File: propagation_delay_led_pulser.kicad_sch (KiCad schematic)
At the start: 16 parts, among them J1 Power/Bias In, J4 Pulse Out, U1 ICM7555xB, U2 74AC14, U3 74AHC1G00

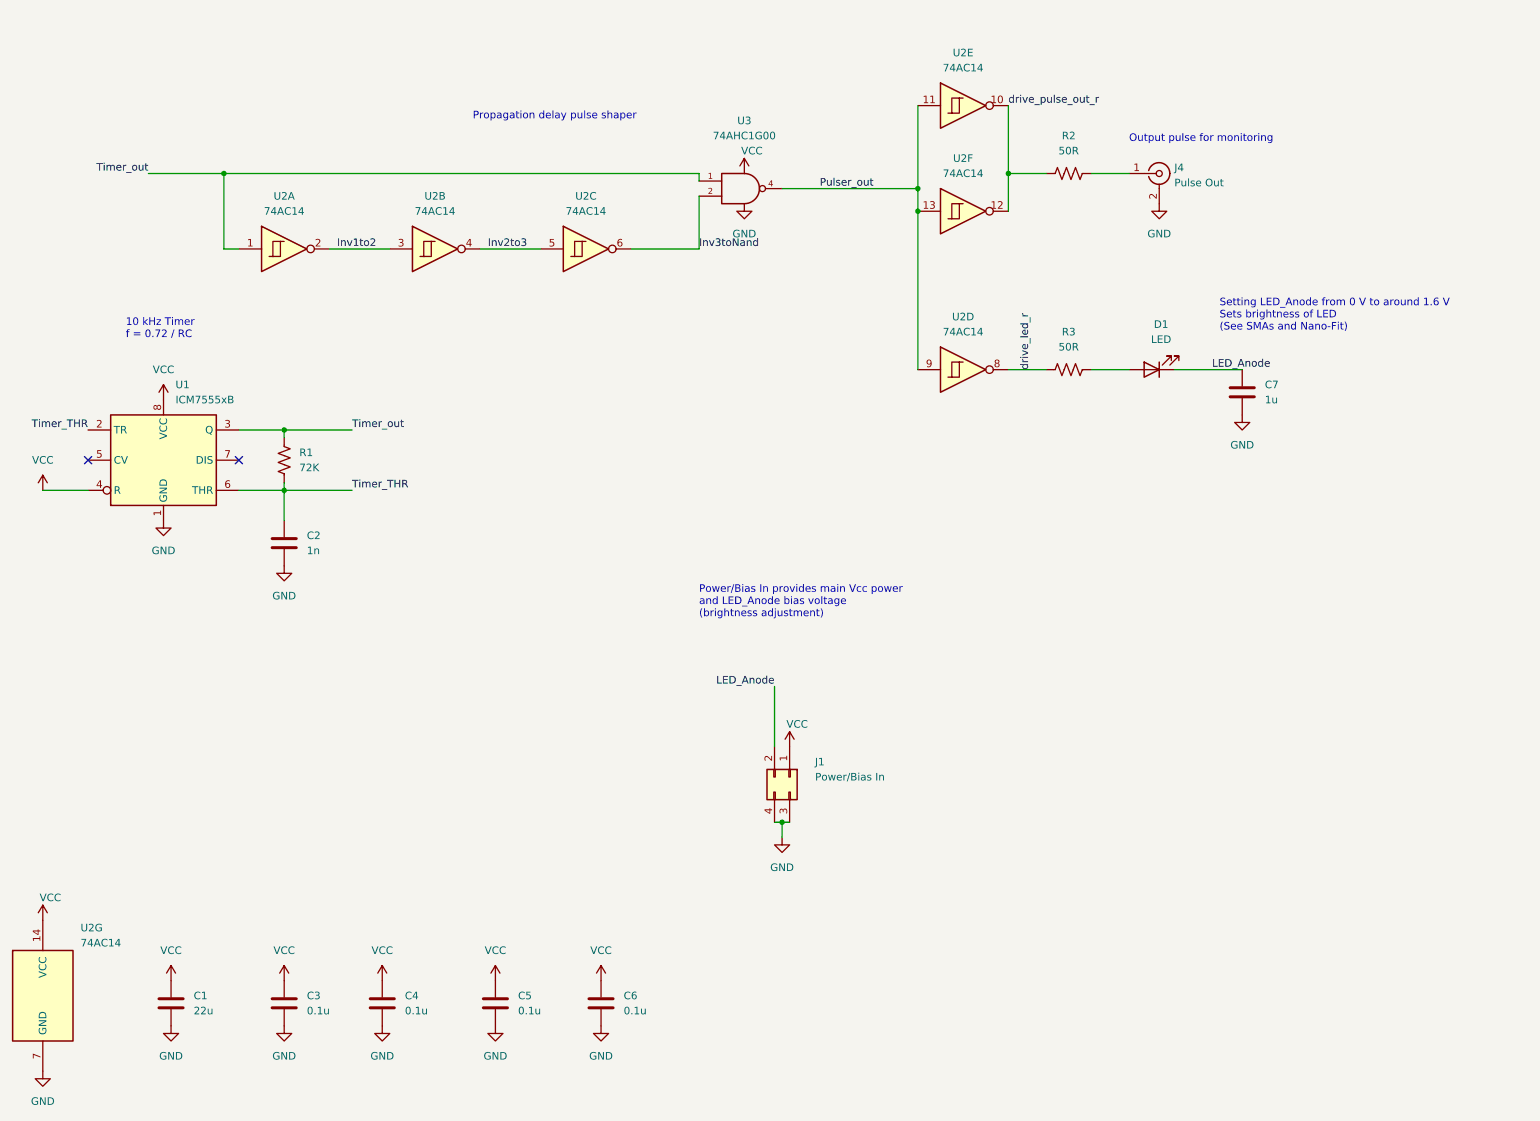
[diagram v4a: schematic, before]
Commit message: most routing done, need to poar ground plane
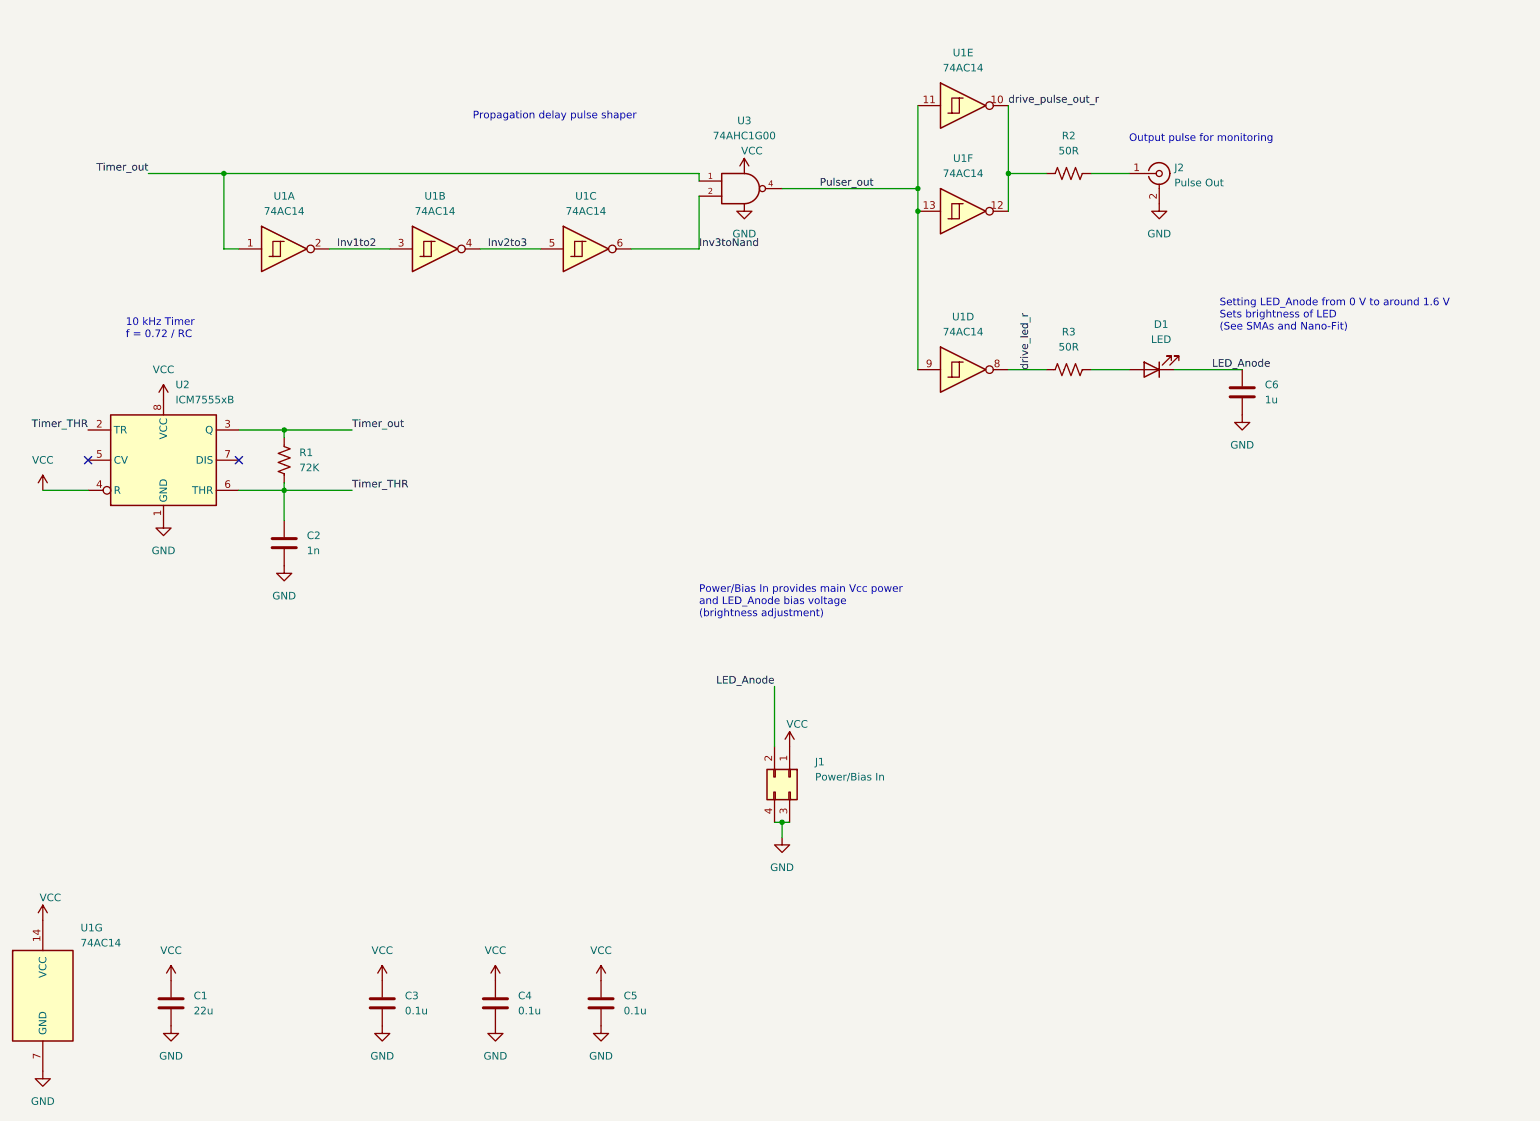
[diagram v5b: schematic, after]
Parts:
- removed C3: 0.1u, Resistor_SMD:R_0612_1632Metric_Pad1.18x3.40mm_HandSolder, symbol Device:C
- U1: renamed from U2; footprint (none) -> Package_SO:SOIC-14_3.9x8.7mm_P1.27mm
- renumbered C4 to C3, C5 to C4, C6 to C5, C7 to C6, J4 to J2, U1 to U2

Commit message: PCB layout complete
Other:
- company: Hugon Labs -> HugonLabs
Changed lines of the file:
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@@
   (title_block
     (title "Propagation Delay LED Pulser")
-    (date "2022-02-21")
-    (rev "v0.1")
-    (company "Hugon Labs")
+    (date "2022-02-28")
+    (rev "1.0")
+    (company "HugonLabs")
   )
   (junction (at 170.18 46.99) (diameter 0) (color 0 0 0 0)

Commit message: Removed extra vias and changed 0612 caps to 1206
  should ease soldering greatly
  Hopefully all done for v1.1
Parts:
- C1: footprint Resistor_SMD:R_1206_3216Metric_Pad1.30x1.75mm_HandSolder -> Capacitor_SMD:C_1206_3216Metric_Pad1.33x1.80mm_HandSolder
- C3, C4, C5: footprint Resistor_SMD:R_0612_1632Metric_Pad1.18x3.40mm_HandSolder -> Capacitor_SMD:C_1206_3216Metric_Pad1.33x1.80mm_HandSolder; Mfr Kyocera AVX -> Samsung; Part 06125C104KAT2A -> CL31B104KBCNNND
- C6: footprint Resistor_SMD:R_0612_1632Metric_Pad1.18x3.40mm_HandSolder -> Capacitor_SMD:C_1206_3216Metric_Pad1.33x1.80mm_HandSolder; Mfr Kyocera AVX -> Samsung; Part 0612YC105KAT2A -> CL31B105KBHNFNE
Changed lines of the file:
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@@
   (title_block
     (title "Propagation Delay LED Pulser")
-    (date "2022-02-28")
-    (rev "1.0")
+    (date "2022-04-12")
+    (rev "1.1")
     (company "HugonLabs")
   )
@@
       (effects (font (size 1.27 1.27)) hide)
     )
+    (pin "1")
+    (pin "2")
+    (pin "3")
+    (pin "4")
+    (pin "5")
+    (pin "6")
+    (pin "8")
+    (pin "9")
+    (pin "10")
+    (pin "11")
     (pin "12")
     (pin "13")
+    (pin "14")
+    (pin "7")
   )
   (symbol (lib_id "power:GND") (at 140.97 45.72 0) (unit 1)
@@
       (effects (font (size 1.27 1.27)) (justify left))
     )
-    (property "Footprint" "Resistor_SMD:R_0612_1632Metric_Pad1.18x3.40mm_HandSolder" (id 2) (at 225.7552 81.28 0)
-      (effects (font (size 1.27 1.27)) hide)
-    )
-    (property "Datasheet" "https://www.mouser.com/datasheet/2/40/AVXCS06407_1-2538087.pdf" (id 3) (at 224.79 77.47 0)
-      (effects (font (size 1.27 1.27)) hide)
-    )
-    (property "Mfr" "Kyocera AVX" (id 4) (at 224.79 77.47 0)
-      (effects (font (size 1.27 1.27)) hide)
-    )
-    (property "Part" "0612YC105KAT2A" (id 5) (at 224.79 77.47 0)
+    (property "Footprint" "Capacitor_SMD:C_1206_3216Metric_Pad1.33x1.80mm_HandSolder" (id 2) (at 225.7552 81.28 0)
+      (effects (font (size 1.27 1.27)) hide)
+    )
+    (property "Datasheet" "https://www.mouser.com/datasheet/2/585/MLCC-1837944.pdf" (id 3) (at 224.79 77.47 0)
+      (effects (font (size 1.27 1.27)) hide)
+    )
+    (property "Mfr" "Samsung" (id 4) (at 224.79 77.47 0)
+      (effects (font (size 1.27 1.27)) hide)
+    )
+    (property "Part" "CL31B105KBHNFNE" (id 5) (at 224.79 77.47 0)
       (effects (font (size 1.27 1.27)) hide)
     )
@@
     (pin "1")
     (pin "2")
+    (pin "3")
+    (pin "4")
+    (pin "5")
+    (pin "6")
+    (pin "8")
+    (pin "9")
+    (pin "10")
+    (pin "11")
+    (pin "12")
+    (pin "13")
+    (pin "14")
+    (pin "7")
   )
   (symbol (lib_id "power:VCC") (at 22.86 166.37 0) (unit 1)
@@
       (effects (font (size 1.27 1.27)) hide)
     )
+    (pin "1")
+    (pin "2")
+    (pin "3")
+    (pin "4")
+    (pin "5")
+    (pin "6")
     (pin "8")
     (pin "9")
+    (pin "10")
+    (pin "11")
+    (pin "12")
+    (pin "13")
+    (pin "14")
+    (pin "7")
   )
   (symbol (lib_id "74xx:74HC14") (at 114.3 53.34 0) (unit 3)
@@
       (effects (font (size 1.27 1.27)) hide)
     )
+    (pin "1")
+    (pin "2")
+    (pin "3")
+    (pin "4")
     (pin "5")
     (pin "6")
+    (pin "8")
+    (pin "9")
+    (pin "10")
+    (pin "11")
+    (pin "12")
+    (pin "13")
+    (pin "14")
+    (pin "7")
   )
   (symbol (lib_id "power:VCC") (at 99.06 176.53 0) (unit 1)
@@
       (effects (font (size 1.27 1.27)) hide)
     )
+    (pin "1")
+    (pin "2")
     (pin "3")
     (pin "4")
+    (pin "5")
+    (pin "6")
+    (pin "8")
+    (pin "9")
+    (pin "10")
+    (pin "11")
+    (pin "12")
+    (pin "13")
+    (pin "14")
+    (pin "7")
   )
   (symbol (lib_id "power:GND") (at 99.06 184.15 0) (unit 1)
@@
       (effects (font (size 1.27 1.27)) (justify left))
     )
-    (property "Footprint" "Resistor_SMD:R_0612_1632Metric_Pad1.18x3.40mm_HandSolder" (id 2) (at 80.9752 184.15 0)
-      (effects (font (size 1.27 1.27)) hide)
-    )
-    (property "Datasheet" "https://www.mouser.com/datasheet/2/40/AVXCS06407_1-2538087.pdf" (id 3) (at 80.01 180.34 0)
-      (effects (font (size 1.27 1.27)) hide)
-    )
-    (property "Mfr" "Kyocera AVX" (id 4) (at 80.01 180.34 0)
-      (effects (font (size 1.27 1.27)) hide)
-    )
-    (property "Part" "06125C104KAT2A" (id 5) (at 80.01 180.34 0)
+    (property "Footprint" "Capacitor_SMD:C_1206_3216Metric_Pad1.33x1.80mm_HandSolder" (id 2) (at 80.9752 184.15 0)
+      (effects (font (size 1.27 1.27)) hide)
+    )
+    (property "Datasheet" "https://www.mouser.com/datasheet/2/585/MLCC-1837944.pdf" (id 3) (at 80.01 180.34 0)
+      (effects (font (size 1.27 1.27)) hide)
+    )
+    (property "Mfr" "Samsung" (id 4) (at 80.01 180.34 0)
+      (effects (font (size 1.27 1.27)) hide)
+    )
+    (property "Part" "CL31B104KBCNNND" (id 5) (at 80.01 180.34 0)
       (effects (font (size 1.27 1.27)) hide)
     )
@@
       (effects (font (size 1.27 1.27)) (justify left))
     )
-    (property "Footprint" "Resistor_SMD:R_1206_3216Metric_Pad1.30x1.75mm_HandSolder" (id 2) (at 45.4152 184.15 0)
+    (property "Footprint" "Capacitor_SMD:C_1206_3216Metric_Pad1.33x1.80mm_HandSolder" (id 2) (at 45.4152 184.15 0)
       (effects (font (size 1.27 1.27)) hide)
     )
@@
       (effects (font (size 1.27 1.27)) (justify left))
     )
-    (property "Footprint" "Resistor_SMD:R_0612_1632Metric_Pad1.18x3.40mm_HandSolder" (id 2) (at 100.0252 184.15 0)
-      (effects (font (size 1.27 1.27)) hide)
-    )
-    (property "Datasheet" "https://www.mouser.com/datasheet/2/40/AVXCS06407_1-2538087.pdf" (id 3) (at 99.06 180.34 0)
-      (effects (font (size 1.27 1.27)) hide)
-    )
-    (property "Mfr" "Kyocera AVX" (id 4) (at 99.06 180.34 0)
-      (effects (font (size 1.27 1.27)) hide)
-    )
-    (property "Part" "06125C104KAT2A" (id 5) (at 99.06 180.34 0)
+    (property "Footprint" "Capacitor_SMD:C_1206_3216Metric_Pad1.33x1.80mm_HandSolder" (id 2) (at 100.0252 184.15 0)
+      (effects (font (size 1.27 1.27)) hide)
+    )
+    (property "Datasheet" "https://www.mouser.com/datasheet/2/585/MLCC-1837944.pdf" (id 3) (at 99.06 180.34 0)
+      (effects (font (size 1.27 1.27)) hide)
+    )
+    (property "Mfr" "Samsung" (id 4) (at 99.06 180.34 0)
+      (effects (font (size 1.27 1.27)) hide)
+    )
+    (property "Part" "CL31B104KBCNNND" (id 5) (at 99.06 180.34 0)
       (effects (font (size 1.27 1.27)) hide)
     )
@@
       (effects (font (size 1.27 1.27)) hide)
     )
+    (pin "1")
+    (pin "2")
+    (pin "3")
+    (pin "4")
+    (pin "5")
+    (pin "6")
+    (pin "8")
+    (pin "9")
+    (pin "10")
+    (pin "11")
+    (pin "12")
+    (pin "13")
     (pin "14")
     (pin "7")
@@
       (effects (font (size 1.27 1.27)) hide)
     )
+    (pin "1")
+    (pin "2")
+    (pin "3")
+    (pin "4")
+    (pin "5")
+    (pin "6")
+    (pin "8")
+    (pin "9")
     (pin "10")
     (pin "11")
+    (pin "12")
+    (pin "13")
+    (pin "14")
+    (pin "7")
   )
   (symbol (lib_id "Device:C") (at 63.5 102.87 0) (unit 1)
@@
       (effects (font (size 1.27 1.27)) (justify left))
     )
-    (property "Footprint" "Resistor_SMD:R_0612_1632Metric_Pad1.18x3.40mm_HandSolder" (id 2) (at 117.8052 184.15 0)
-      (effects (font (size 1.27 1.27)) hide)
-    )
-    (property "Datasheet" "https://www.mouser.com/datasheet/2/40/AVXCS06407_1-2538087.pdf" (id 3) (at 116.84 180.34 0)
-      (effects (font (size 1.27 1.27)) hide)
-    )
-    (property "Mfr" "Kyocera AVX" (id 4) (at 116.84 180.34 0)
-      (effects (font (size 1.27 1.27)) hide)
-    )
-    (property "Part" "06125C104KAT2A" (id 5) (at 116.84 180.34 0)
+    (property "Footprint" "Capacitor_SMD:C_1206_3216Metric_Pad1.33x1.80mm_HandSolder" (id 2) (at 117.8052 184.15 0)
+      (effects (font (size 1.27 1.27)) hide)
+    )
+    (property "Datasheet" "https://www.mouser.com/datasheet/2/585/MLCC-1837944.pdf" (id 3) (at 116.84 180.34 0)
+      (effects (font (size 1.27 1.27)) hide)
+    )
+    (property "Mfr" "Samsung" (id 4) (at 116.84 180.34 0)
+      (effects (font (size 1.27 1.27)) hide)
+    )
+    (property "Part" "CL31B104KBCNNND" (id 5) (at 116.84 180.34 0)
       (effects (font (size 1.27 1.27)) hide)
     )
@@
     )
     (path "/5b86cb50-e2ef-475e-93e3-77fea6b5a690"
-      (reference "C1") (unit 1) (value "22u") (footprint "Resistor_SMD:R_1206_3216Metric_Pad1.30x1.75mm_HandSolder")
+      (reference "C1") (unit 1) (value "22u") (footprint "Capacitor_SMD:C_1206_3216Metric_Pad1.33x1.80mm_HandSolder")
     )
     (path "/f2947cd1-32b2-4d7c-98a3-14a6c22abb15"
@@
     )
     (path "/52581d88-1679-4e7a-a5a5-2812add71e96"
-      (reference "C3") (unit 1) (value "0.1u") (footprint "Resistor_SMD:R_0612_1632Metric_Pad1.18x3.40mm_HandSolder")
+      (reference "C3") (unit 1) (value "0.1u") (footprint "Capacitor_SMD:C_1206_3216Metric_Pad1.33x1.80mm_HandSolder")
     )
     (path "/a312de14-abf2-4a98-a2e6-2cdd154c1f42"
-      (reference "C4") (unit 1) (value "0.1u") (footprint "Resistor_SMD:R_0612_1632Metric_Pad1.18x3.40mm_HandSolder")
+      (reference "C4") (unit 1) (value "0.1u") (footprint "Capacitor_SMD:C_1206_3216Metric_Pad1.33x1.80mm_HandSolder")
     )
     (path "/f722116b-5e49-4401-8f1c-5aad01f0ac9f"
-      (reference "C5") (unit 1) (value "0.1u") (footprint "Resistor_SMD:R_0612_1632Metric_Pad1.18x3.40mm_HandSolder")
+      (reference "C5") (unit 1) (value "0.1u") (footprint "Capacitor_SMD:C_1206_3216Metric_Pad1.33x1.80mm_HandSolder")
     )
     (path "/1482cc50-83d2-496d-8746-c45fa584deec"
-      (reference "C6") (unit 1) (value "1u") (footprint "Resistor_SMD:R_0612_1632Metric_Pad1.18x3.40mm_HandSolder")
+      (reference "C6") (unit 1) (value "1u") (footprint "Capacitor_SMD:C_1206_3216Metric_Pad1.33x1.80mm_HandSolder")
     )
     (path "/6677affe-2cba-4052-88eb-c739b0e26076"
